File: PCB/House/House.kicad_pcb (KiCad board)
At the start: 2 copper layers, 95 x 60.5 mm, 37 parts, among them J1 Conn_01x05, U1 HT16K33-28SOP

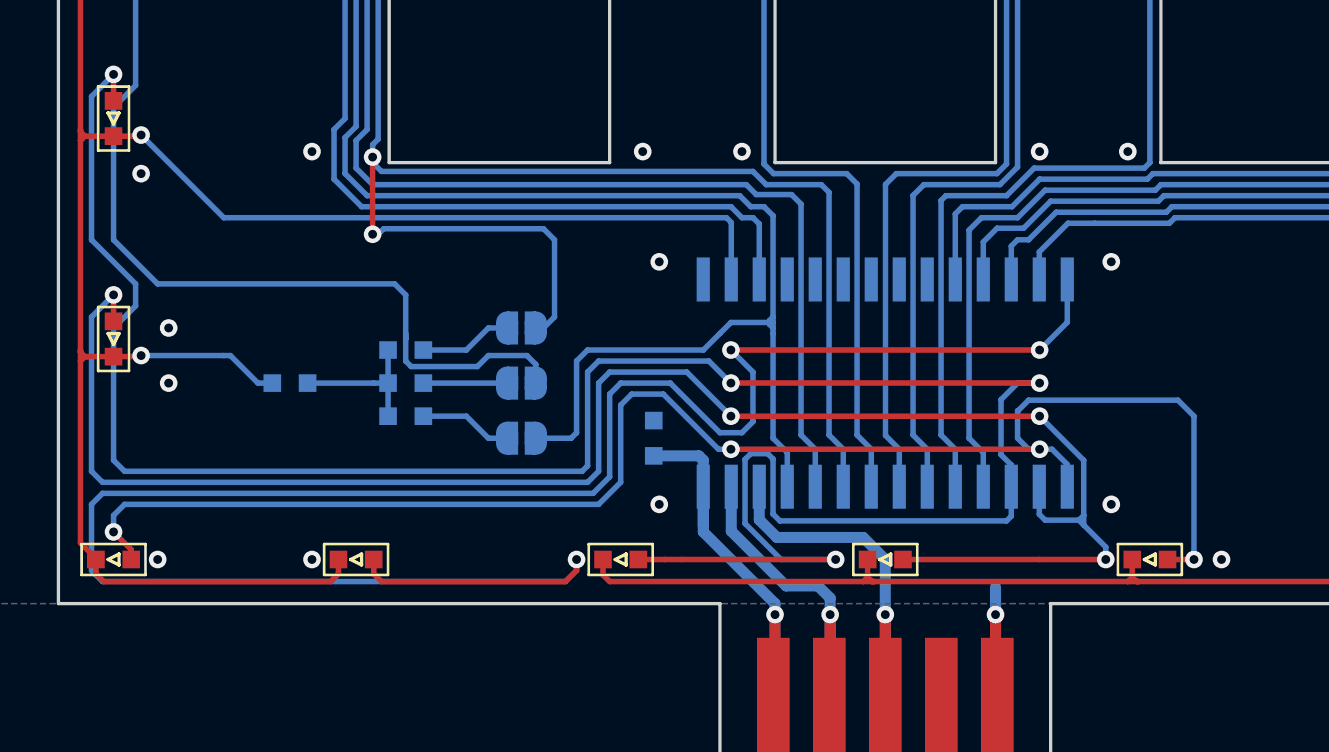
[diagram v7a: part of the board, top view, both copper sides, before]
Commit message: [update] Houseの配線改善(ICの横4本配線の位置の中心化)
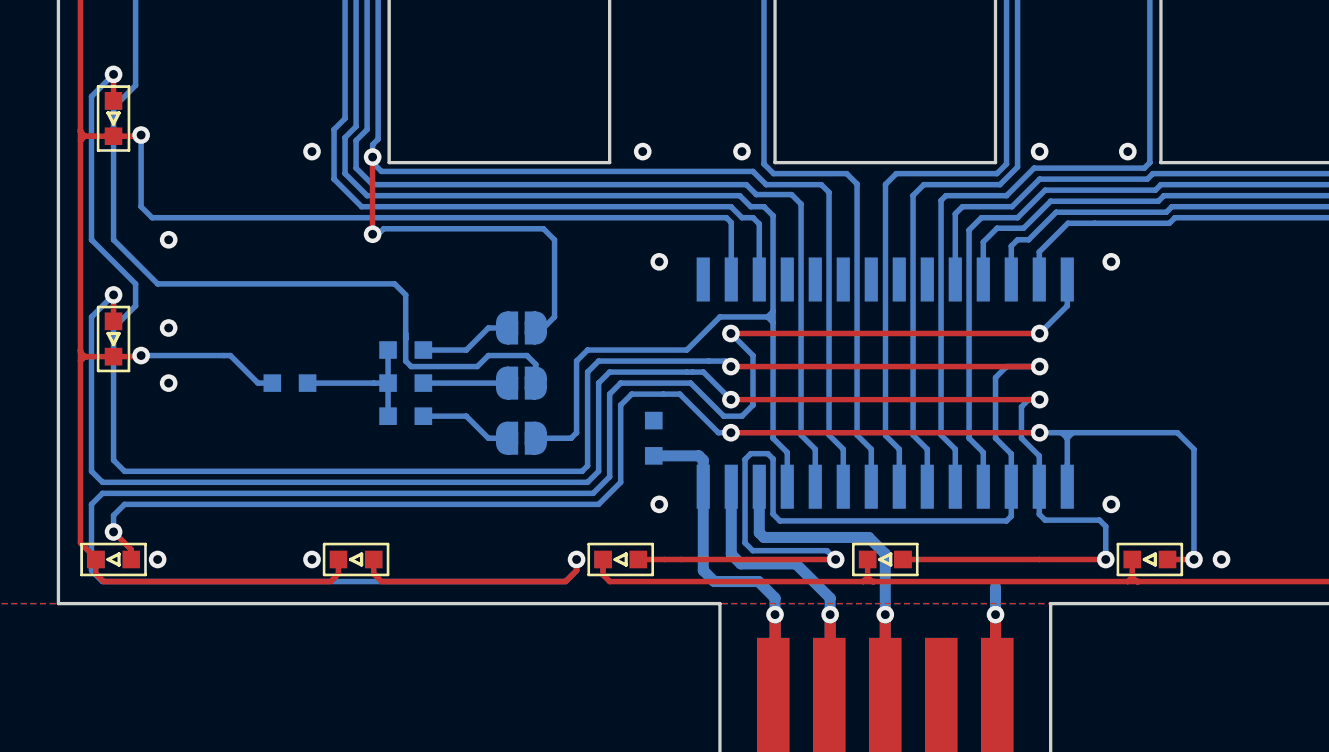
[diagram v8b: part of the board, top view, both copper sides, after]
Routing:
- net Net-(D11-Pad2): track 70.9 -> 66.8 mm
- net Net-(D1-Pad1): track 311.2 -> 313.1 mm
- net Net-(D25-Pad2): track 106.7 -> 108.2 mm
- net Net-(D12-Pad2): track 93.9 -> 92.8 mm
- net Net-(D10-Pad2): track 78.8 -> 77.9 mm
- net +5V: track 23.5 -> 22.9 mm
- net SDA: track 19.5 -> 20.2 mm
